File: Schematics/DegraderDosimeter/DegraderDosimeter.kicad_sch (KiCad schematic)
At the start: 0 parts

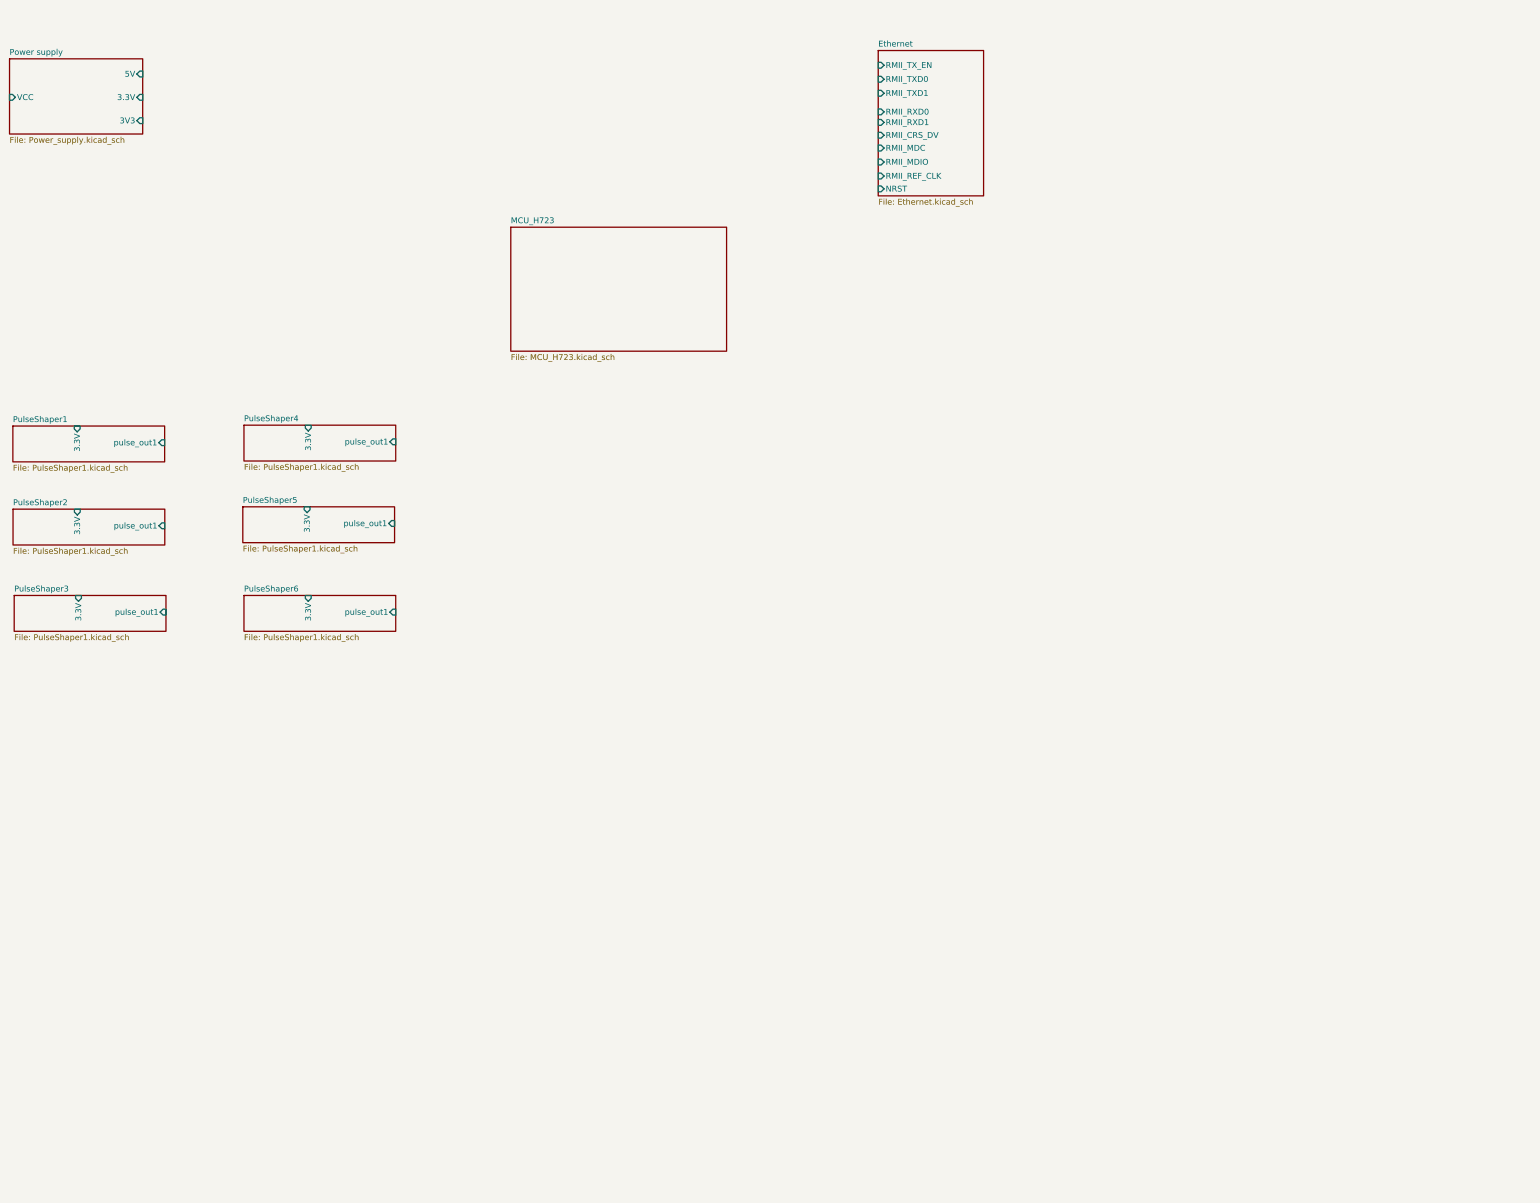
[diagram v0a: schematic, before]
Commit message: Bring the DegraderDosimeter schematic up to a routable state
Single ECAD commit on top of "First upload", carrying both the earlier
board-bring-up work and this session's changes. Squashed here so the
schematic history is separate from the FirmwareUpdate restructure, which
stays on main.

Library resolution
  Register the A4988 and LM60430DRPKR symbol libraries in sym-lib-table,
  and the DE15, DRIVER-A4988SETTR-T_QFN28_ and KRJ-CB4.2GYZNL footprint
  libraries in fp-lib-table. Point H1102NL at ${KIPRJMOD} instead of the
  undefined ${CUSTOM}. All 26 symbols and 24 footprints now resolve.

Degrader to MCU
  Wire all 32 degrader signals to the STM32H723: 11 A4988/L293D controls
  and 21 lens limit switches. Reuse the F746 firmware's pin assignment
  where it does not clash with the dosimeter; MS1 and MS2 move to PD14
  and PD15 because PD11/PD12 are pulse-capture pins, and !ENABLE takes
  PB7 as the firmware never assigned it. Grow the MCU_H723 sheet so its
  right edge spans the Degrader sheet, giving one straight wire per net.

Net naming and classes
  Drop the duplicate port label on the 50 pins that already carry a
  functional hierarchical label, so nets read STEP/MS1/RMII_REF_CLK
  rather than PD14/PA1; unused pins keep their port label and bus. Name
  the remaining 73 auto-named nets. Add ETH_DIFF_100R, ETH_RMII, POWER,
  MOTOR and ANALOG net classes. The four MDI pairs get 0.15 mm track on
  a 0.30 mm gap, which is 100 ohm differential on the declared stackup
  (F.Cu over In1.Cu, 0.1 mm prepreg, er 4.5) - reconfirm if the fab
  ships a different stackup.

Connection fixes
  - MDC/MDIO were crossed: PA2 landed on the PHY's MDC pin and PC1 on
    MDIO. Swapped the two labels in Ethernet.kicad_sch.
  - PULSE_6 moved PD11 -> PD12, the TIM4_CH1 pin BLM_Code.ioc expects.
  - PulseShaper 1, 2 and 5 outputs missed their sheet pins by 2-81 um.
  - XTAL1 stopped 0.254 mm short of Y1/C1, leaving the PHY crystal open.
  - C32/C35 and C39/C40, the U5 and U7 cap returns, h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
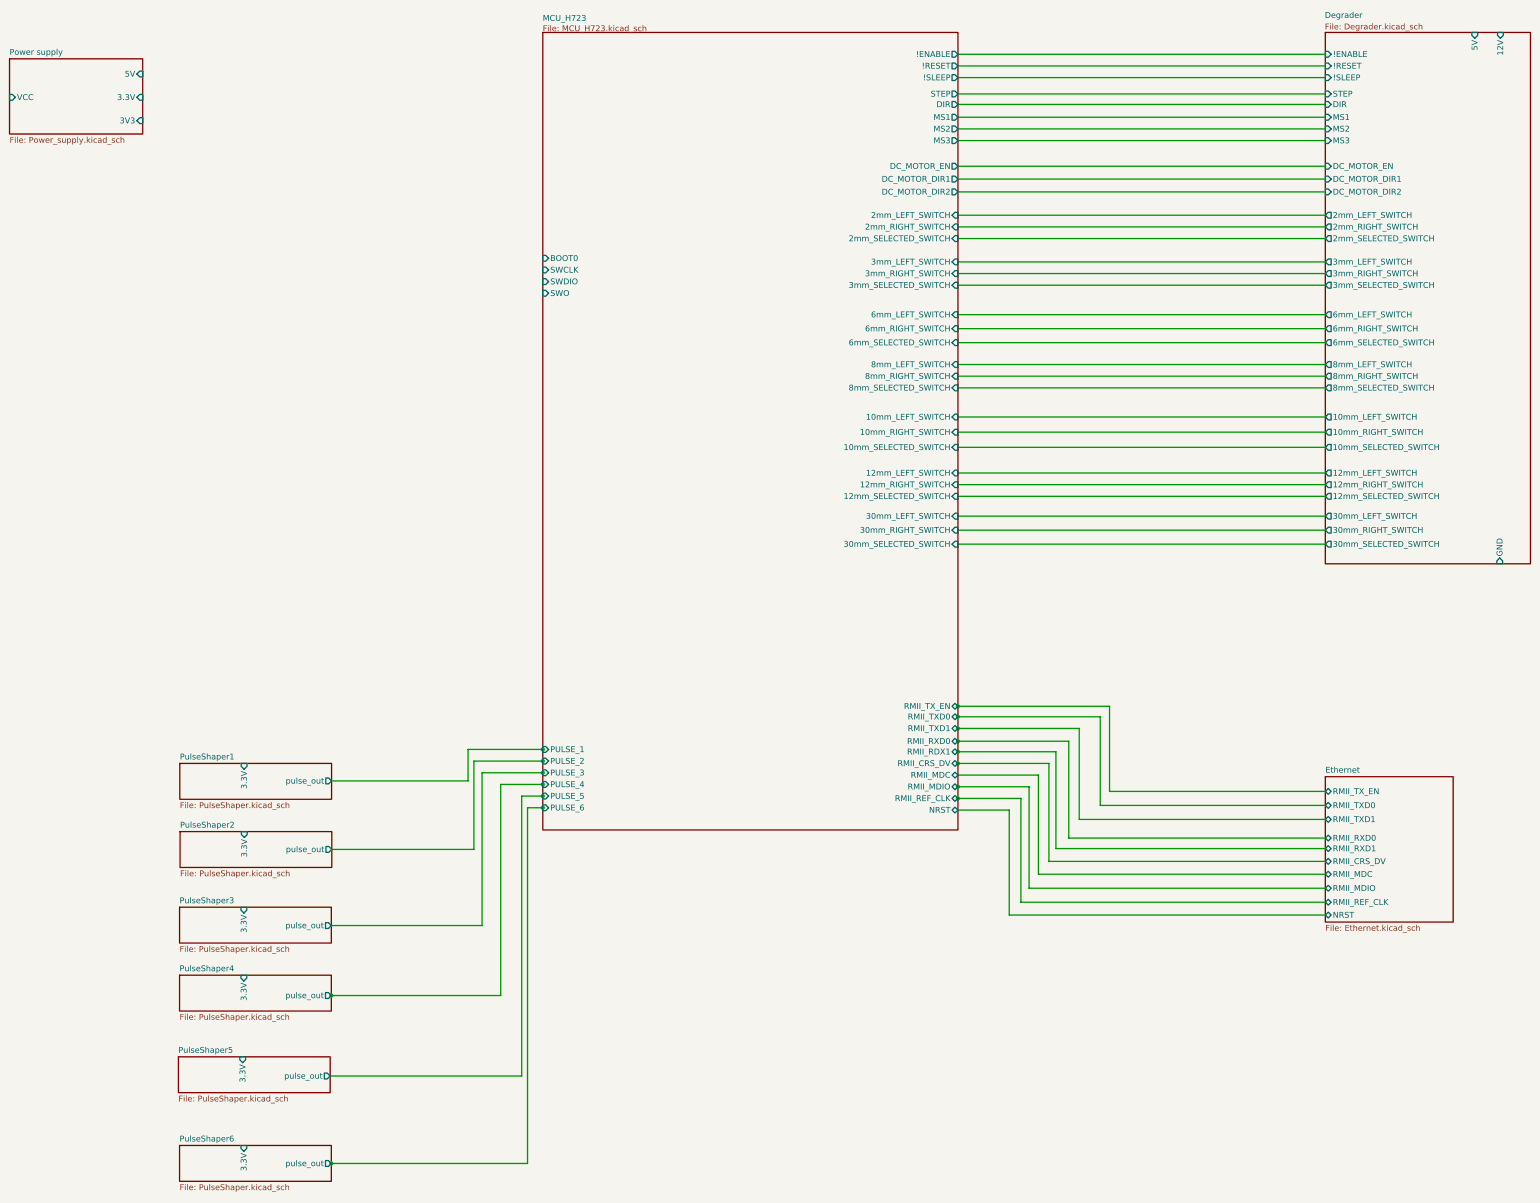
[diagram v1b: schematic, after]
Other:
- added sheet Degrader (Degrader.kicad_sch)
- sheet MCU_H723 ports: added !ENABLE, !RESET, !SLEEP, 10mm_LEFT_SWITCH, 10mm_RIGHT_SWITCH, 10mm_SELECTED_SWITCH, 12mm_LEFT_SWITCH, 12mm_RIGHT_SWITCH, 12mm_SELECTED_SWITCH, 2mm_LEFT_SWITCH, 2mm_RIGHT_SWITCH, 2mm_SELECTED_SWITCH, 30mm_LEFT_SWITCH, 30mm_RIGHT_SWITCH, 30mm_SELECTED_SWITCH, 3mm_LEFT_SWITCH, 3mm_RIGHT_SWITCH, 3mm_SELECTED_SWITCH, 6mm_LEFT_SWITCH, 6mm_RIGHT_SWITCH, 6mm_SELECTED_SWITCH, 8mm_LEFT_SWITCH, 8mm_RIGHT_SWITCH, 8mm_SELECTED_SWITCH, BOOT0, DC_MOTOR_DIR1, DC_MOTOR_DIR2, DC_MOTOR_EN, DIR, MS1, MS2, MS3, NRST, PULSE_1, PULSE_2, PULSE_3, PULSE_4, PULSE_5, PULSE_6, RMII_CRS_DV, RMII_MDC, RMII_MDIO, RMII_RDX1, RMII_REF_CLK, RMII_RXD0, RMII_TXD0, RMII_TXD1, RMII_TX_EN, STEP, SWCLK, SWDIO, SWO; removed none
- sheet PulseShaper1: file PulseShaper1.kicad_sch -> PulseShaper.kicad_sch
- sheet PulseShaper1 ports: added pulse_out; removed pulse_out1
- sheet PulseShaper2: file PulseShaper1.kicad_sch -> PulseShaper.kicad_sch
- sheet PulseShaper2 ports: added pulse_out; removed pulse_out1
- sheet PulseShaper3: file PulseShaper1.kicad_sch -> PulseShaper.kicad_sch
- sheet PulseShaper3 ports: added pulse_out; removed pulse_out1
- sheet PulseShaper4: file PulseShaper1.kicad_sch -> PulseShaper.kicad_sch
- sheet PulseShaper4 ports: added pulse_out; removed pulse_out1
- sheet PulseShaper5: file PulseShaper1.kicad_sch -> PulseShaper.kicad_sch
- sheet PulseShaper5 ports: added pulse_out; removed pulse_out1
- sheet PulseShaper6: file PulseShaper1.kicad_sch -> PulseShaper.kicad_sch
- sheet PulseShaper6 ports: added pulse_out; removed pulse_out1
